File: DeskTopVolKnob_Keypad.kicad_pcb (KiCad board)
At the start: 2 copper layers, 118.4 x 101.6 mm, 108 parts, among them J1 DX07S016JA1R1500, SW1 Rotary_Encoder_Switch, SW10 SW, SW11 SW, SW12 SW, SW13 SW, SW14 SW, SW15 SW, SW16 SW, SW17 SW, SW18 SW, SW19 SW, SW2 SW, SW20 SW, SW21 SW, SW22 SW, SW23 SW, SW24 SW, SW25 SW, SW26 SW, SW27 SW_Push, SW3 SW, SW4 SW, SW5 SW, SW6 SW, SW7 SW, SW8 SW, SW9 SW, U1 ATmega32U4-AU, Y1 16MHz

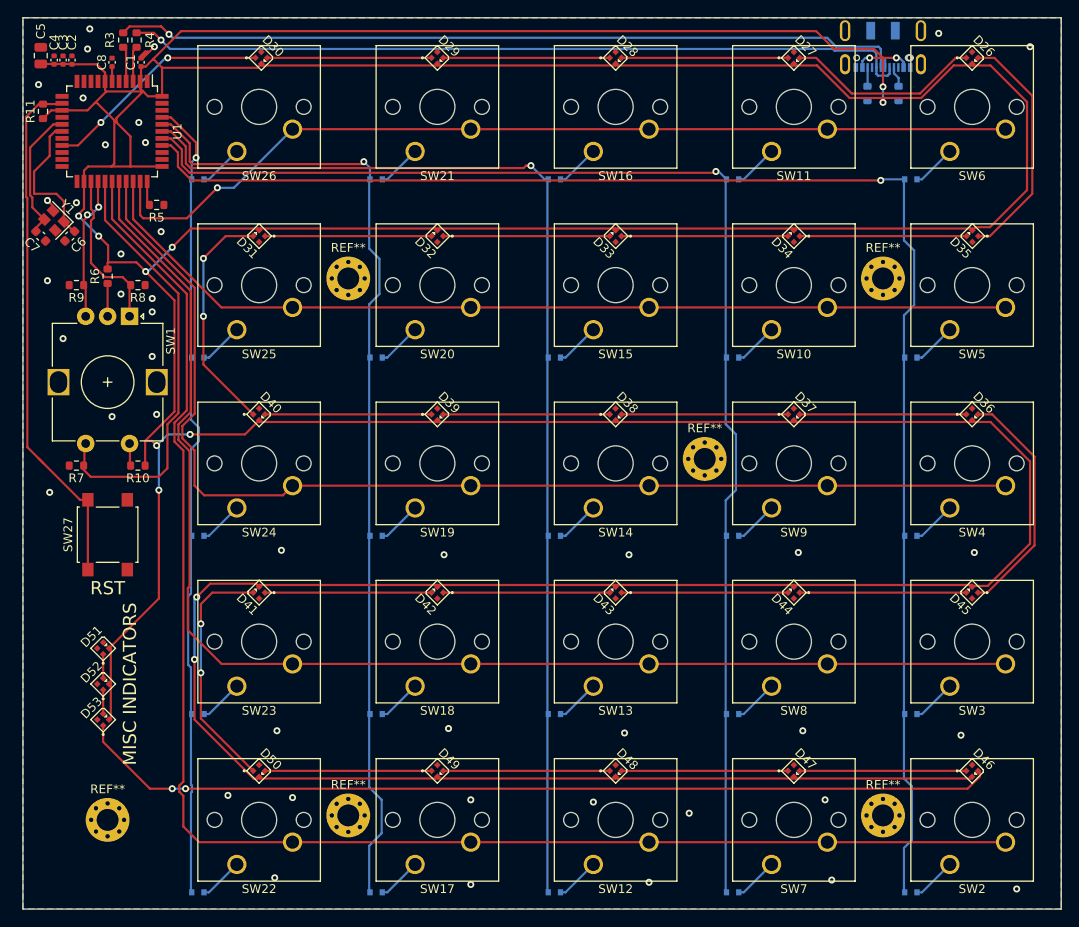
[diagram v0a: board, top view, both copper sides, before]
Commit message: LEDs redesigned for ili controller
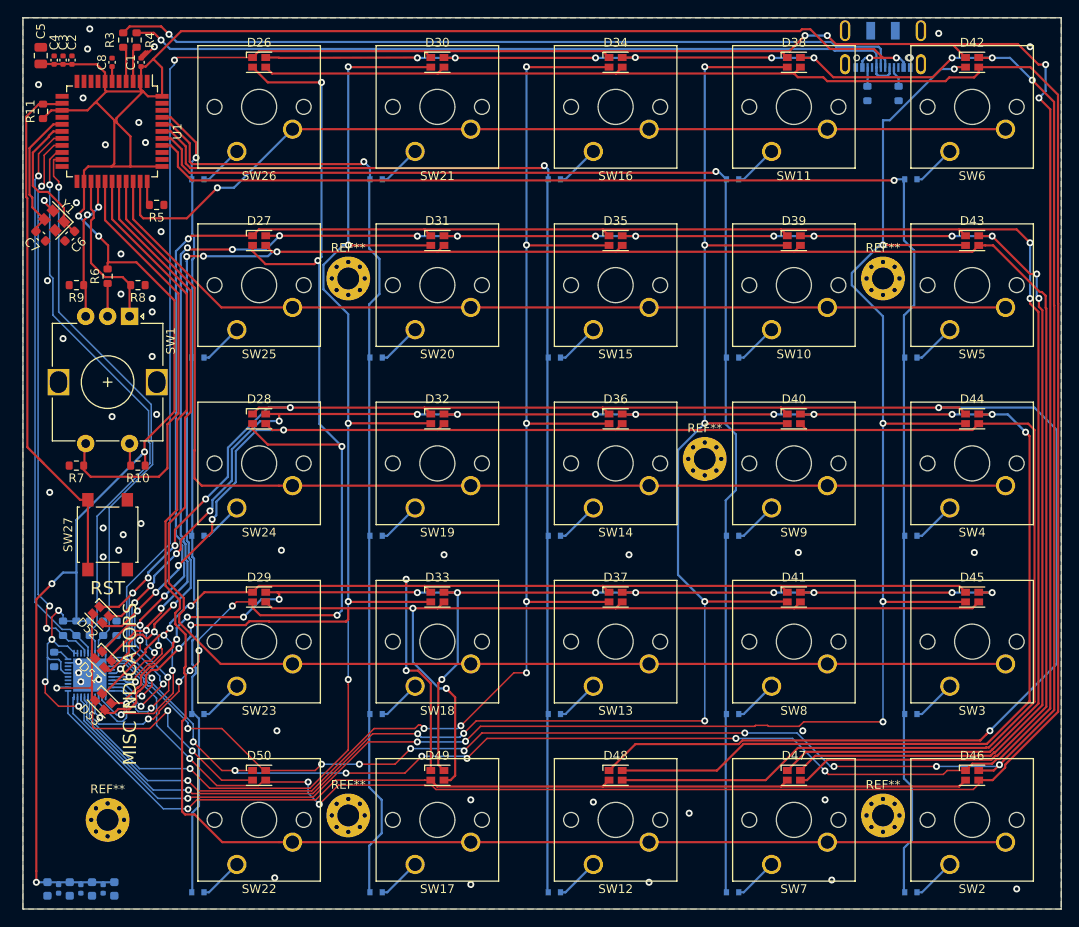
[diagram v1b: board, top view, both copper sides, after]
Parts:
- added C10: 0.1uF, Capacitor_SMD:C_0402_1005Metric, B.Cu at (43.2, 127.3)
- added C11: 0.47uF, Capacitor_SMD:C_0603_1608Metric, B.Cu at (44.5, 127.3)
- added C12: 0.1uF, Capacitor_SMD:C_0402_1005Metric, B.Cu at (40.6, 127.3)
- added C13: 0.47uF, Capacitor_SMD:C_0603_1608Metric, B.Cu at (47.0, 127.3)
- added C14: 0.1uF, Capacitor_SMD:C_0402_1005Metric, B.Cu at (45.7, 127.3)
- added C15: 0.47uF, Capacitor_SMD:C_0603_1608Metric, B.Cu at (41.9, 127.3)
- added C9: 0.47uF, Capacitor_SMD:C_0603_1608Metric, B.Cu at (39.4, 127.3)
- added R12: 4.7k, Resistor_SMD:R_0603_1608Metric, B.Cu at (41.1, 97.5)
- added R13: 100k, Resistor_SMD:R_0603_1608Metric, B.Cu at (45.7, 97.5)
- added R14: 100k, Resistor_SMD:R_0603_1608Metric, B.Cu at (47.2, 97.5)
- added R15: 4.7k, Resistor_SMD:R_0603_1608Metric, B.Cu at (42.7, 97.5)
- added R16: 100k, Resistor_SMD:R_0603_1608Metric, B.Cu at (44.2, 97.5)
- added R17: 20k, Resistor_SMD:R_0603_1608Metric, B.Cu at (40.1, 101.1)
- added U2: IS31FL3737, Package_DFN_QFN:QFN-40-1EP_5x5mm_P0.4mm_EP3.8x3.8mm, B.Cu at (44.2, 102.9)
- D26, D27, D28, D29, D30, D31, D32, D33, D34, D35, D36, D37, D38, D39, D40, D41, D42, D43, D44, D45, D46, D47, D48, D49, D50, D51, D52, D53: value SK6805-EC-15 -> LED_RGBA; footprint Special Partd:SK6805-EC-15 -> LED_SMD:LED_Cree-PLCC4_2x2mm_CW
- moved D42 85.9 mm to (144.8, 33.0), turned to 0 degrees
- moved D26 81.3 mm to (63.5, 33.0), turned to 0 degrees
- moved D29 64.7 mm to (63.5, 94.0), turned to 0 degrees
- moved D27 64.4 mm to (63.5, 53.3), turned to 0 degrees
- moved D40 61.0 mm to (124.5, 73.7), turned to 0 degrees
- moved D41 61.0 mm to (124.5, 94.0), turned to 0 degrees
- moved D28 57.8 mm to (63.5, 73.7), turned to 0 degrees
- moved D43 57.1 mm to (144.8, 53.3), turned to 0 degrees
- moved D33 45.9 mm to (83.8, 94.0), turned to 0 degrees
- moved D39 45.2 mm to (124.5, 53.3), turned to 0 degrees
- moved D38 45.0 mm to (124.5, 33.0), turned to 0 degrees
- moved D35 40.7 mm to (104.1, 53.3), turned to 0 degrees
- moved D36 40.6 mm to (104.1, 73.7), turned to 0 degrees
- moved D37 29.1 mm to (104.1, 94.0), turned to 0 degrees
- moved D44 28.4 mm to (144.8, 73.7), turned to 0 degrees
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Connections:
- D26 pad 2: +5V -> Net-(D26-Pad2)
- D26 pad 4: GND -> Net-(D26-Pad4)
- D27 pad 2: +5V -> Net-(D27-Pad2)
- D27 pad 3: Net-(D26-Pad1) -> Net-(D27-Pad3)
- D27 pad 4: GND -> Net-(D26-Pad4)
- D28 pad 2: +5V -> Net-(D28-Pad2)
- D28 pad 3: Net-(D27-Pad1) -> Net-(D28-Pad3)
- D28 pad 4: GND -> Net-(D26-Pad4)
- D29 pad 2: +5V -> Net-(D29-Pad2)
- D29 pad 3: Net-(D28-Pad1) -> Net-(D29-Pad3)
- D29 pad 4: GND -> Net-(D26-Pad4)
- D30 pad 1: /LEDs/SD -> Net-(D26-Pad1)
- D30 pad 2: +5V -> Net-(D26-Pad2)
- D30 pad 3: Net-(D29-Pad1) -> Net-(D26-Pad3)
- D30 pad 4: GND -> Net-(D30-Pad4)
- D31 pad 1: Net-(D31-Pad1) -> Net-(D27-Pad1)
- D31 pad 2: +5V -> Net-(D27-Pad2)
- D31 pad 3: Net-(D31-Pad3) -> Net-(D27-Pad3)
- D31 pad 4: GND -> Net-(D30-Pad4)
- D32 pad 1: Net-(D32-Pad1) -> Net-(D28-Pad1)
- D32 pad 2: +5V -> Net-(D28-Pad2)
- D32 pad 3: Net-(D31-Pad1) -> Net-(D28-Pad3)
- D32 pad 4: GND -> Net-(D30-Pad4)
- D33 pad 1: Net-(D33-Pad1) -> Net-(D29-Pad1)
- D33 pad 2: +5V -> Net-(D29-Pad2)
- D33 pad 3: Net-(D32-Pad1) -> Net-(D29-Pad3)
- D33 pad 4: GND -> Net-(D30-Pad4)
- D34 pad 1: Net-(D34-Pad1) -> Net-(D26-Pad1)
- D34 pad 2: +5V -> Net-(D26-Pad2)
- D34 pad 3: Net-(D33-Pad1) -> Net-(D26-Pad3)
- D34 pad 4: GND -> Net-(D34-Pad4)
- D35 pad 1: Net-(D26-Pad3) -> Net-(D27-Pad1)
- D35 pad 2: +5V -> Net-(D27-Pad2)
- D35 pad 3: Net-(D34-Pad1) -> Net-(D27-Pad3)
- D35 pad 4: GND -> Net-(D34-Pad4)
- D36 pad 1: Net-(D36-Pad1) -> Net-(D28-Pad1)
- D36 pad 2: +5V -> Net-(D28-Pad2)
- D36 pad 3: Net-(D36-Pad3) -> Net-(D28-Pad3)
- D36 pad 4: GND -> Net-(D34-Pad4)
- D37 pad 1: Net-(D37-Pad1) -> Net-(D29-Pad1)
- D37 pad 2: +5V -> Net-(D29-Pad2)
- D37 pad 3: Net-(D36-Pad1) -> Net-(D29-Pad3)
- D37 pad 4: GND -> Net-(D34-Pad4)
- D38 pad 1: Net-(D38-Pad1) -> Net-(D26-Pad1)
- D38 pad 2: +5V -> Net-(D26-Pad2)
- D38 pad 3: Net-(D37-Pad1) -> Net-(D26-Pad3)
- D38 pad 4: GND -> Net-(D38-Pad4)
- D39 pad 1: Net-(D39-Pad1) -> Net-(D27-Pad1)
- D39 pad 2: +5V -> Net-(D27-Pad2)
- D39 pad 3: Net-(D38-Pad1) -> Net-(D27-Pad3)
- D39 pad 4: GND -> Net-(D38-Pad4)
- D40 pad 1: Net-(D31-Pad3) -> Net-(D28-Pad1)
- D40 pad 2: +5V -> Net-(D28-Pad2)
- D40 pad 3: Net-(D39-Pad1) -> Net-(D28-Pad3)
- D40 pad 4: GND -> Net-(D38-Pad4)
- D41 pad 1: Net-(D41-Pad1) -> Net-(D29-Pad1)
- D41 pad 2: +5V -> Net-(D29-Pad2)
- D41 pad 3: Net-(D41-Pad3) -> Net-(D29-Pad3)
- D41 pad 4: GND -> Net-(D38-Pad4)
- D42 pad 1: Net-(D42-Pad1) -> Net-(D26-Pad1)
- D42 pad 2: +5V -> Net-(D26-Pad2)
- D42 pad 3: Net-(D41-Pad1) -> Net-(D26-Pad3)
- D42 pad 4: GND -> Net-(D42-Pad4)
- D43 pad 1: Net-(D43-Pad1) -> Net-(D27-Pad1)
- D43 pad 2: +5V -> Net-(D27-Pad2)
- D43 pad 3: Net-(D42-Pad1) -> Net-(D27-Pad3)
- D43 pad 4: GND -> Net-(D42-Pad4)
- D44 pad 1: Net-(D44-Pad1) -> Net-(D28-Pad1)
- D44 pad 2: +5V -> Net-(D28-Pad2)
- D44 pad 3: Net-(D43-Pad1) -> Net-(D28-Pad3)
- D44 pad 4: GND -> Net-(D42-Pad4)
- D45 pad 1: Net-(D36-Pad3) -> Net-(D29-Pad1)
- D45 pad 2: +5V -> Net-(D29-Pad2)
- D45 pad 3: Net-(D44-Pad1) -> Net-(D29-Pad3)
- D45 pad 4: GND -> Net-(D42-Pad4)
- D46 pad 1: Net-(D46-Pad1) -> Net-(D26-Pad1)
- D46 pad 2: +5V -> Net-(D26-Pad2)
- D46 pad 3: Net-(D46-Pad3) -> Net-(D26-Pad3)
- D46 pad 4: GND -> Net-(D46-Pad4)
- D47 pad 1: Net-(D47-Pad1) -> Net-(D27-Pad1)
- D47 pad 2: +5V -> Net-(D27-Pad2)
- D47 pad 3: Net-(D46-Pad1) -> Net-(D27-Pad3)
- D47 pad 4: GND -> Net-(D46-Pad4)
- D48 pad 1: Net-(D48-Pad1) -> Net-(D28-Pad1)
- D48 pad 2: +5V -> Net-(D28-Pad2)
- D48 pad 3: Net-(D47-Pad1) -> Net-(D28-Pad3)
- D48 pad 4: GND -> Net-(D46-Pad4)
- D49 pad 1: Net-(D49-Pad1) -> Net-(D29-Pad1)
- D49 pad 2: +5V -> Net-(D29-Pad2)
- D49 pad 3: Net-(D48-Pad1) -> Net-(D29-Pad3)
- D49 pad 4: GND -> Net-(D46-Pad4)
- D50 pad 1: Net-(D41-Pad3) -> Net-(D26-Pad1)
- D50 pad 2: +5V -> Net-(D26-Pad2)
- D50 pad 3: Net-(D49-Pad1) -> Net-(D26-Pad3)
- D50 pad 4: GND -> Net-(D50-Pad4)
- D51 pad 1: Net-(D51-Pad1) -> Net-(D27-Pad1)
- D51 pad 2: +5V -> Net-(D27-Pad2)
- D51 pad 3: Net-(D51-Pad3) -> Net-(D27-Pad3)
- D51 pad 4: GND -> Net-(D50-Pad4)
- D52 pad 1: Net-(D52-Pad1) -> Net-(D28-Pad1)
- D52 pad 2: +5V -> Net-(D28-Pad2)
- D52 pad 3: Net-(D51-Pad1) -> Net-(D28-Pad3)
- D52 pad 4: GND -> Net-(D50-Pad4)
- D53 pad 1: Net-(D46-Pad3) -> Net-(D29-Pad1)
- D53 pad 2: +5V -> Net-(D29-Pad2)
- D53 pad 3: Net-(D52-Pad1) -> Net-(D29-Pad3)
- D53 pad 4: GND -> Net-(D50-Pad4)
- U1 pad 18: Net-(U1-Pad18) -> /LEDs/SCL
- U1 pad 19: /LEDs/SD -> /LEDs/SDA
- U1 pad 20: Net-(U1-Pad20) -> /LEDs/INTB
- U1 pad 21: Net-(U1-Pad21) -> /LEDs/SDB
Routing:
- net +5V: track 775.1 -> 295.0 mm, vias 13 -> 11
- net Net-(D26-Pad1): track 22.3 -> 374.6 mm, vias 0 -> 12
- net Net-(D26-Pad2): track 0.00 -> 291.3 mm, vias 0 -> 18
- net Net-(D26-Pad3): track 27.3 -> 289.9 mm, vias 0 -> 3
- net Net-(D27-Pad2): track 0.00 -> 249.2 mm, vias 0 -> 17
- net Net-(D27-Pad3): track 0.00 -> 247.6 mm, vias 0 -> 7
- net Net-(D28-Pad3): track 0.00 -> 227.1 mm, vias 0 -> 7
- net Net-(D27-Pad1): track 19.0 -> 246.0 mm, vias 0 -> 7
- net Net-(D28-Pad2): track 0.00 -> 226.2 mm, vias 0 -> 16
- net Net-(D28-Pad1): track 19.0 -> 234.2 mm, vias 0 -> 9
- net Net-(D42-Pad4): track 0.00 -> 213.9 mm, vias 0 -> 8
- net Net-(D38-Pad4): track 0.00 -> 195.6 mm, vias 0 -> 8
- net Net-(D34-Pad4): track 0.00 -> 168.9 mm, vias 0 -> 8
- net Net-(D30-Pad4): track 0.00 -> 155.4 mm, vias 0 -> 6
- net Net-(D29-Pad3): track 0.00 -> 147.4 mm, vias 0 -> 5
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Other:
- net class Default: clearance 0.2 -> 0.127
- net class min added: clearance 0.127, trace_width 0.1778, via_dia 0.40005, via_drill 0.2
- rule trace_clearance: 0.2 -> 0.127
- rule trace_min: 0.2 -> 0.127
- rule via_min_drill: 0.3 -> 0.2
- rule via_min_size: 0.4 -> 0.40005
